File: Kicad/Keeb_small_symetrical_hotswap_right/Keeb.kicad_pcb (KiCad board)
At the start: 2 copper layers, 96.3 x 99.3 mm, 20 parts, among them J1 TYPE-C-31-M-12, SW1 CherryMX, SW10 CherryMX, SW11 CherryMX, SW13 CherryMX, SW14 CherryMX, SW15 CherryMX, SW16 CherryMX, SW17 CherryMX, SW18 CherryMX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

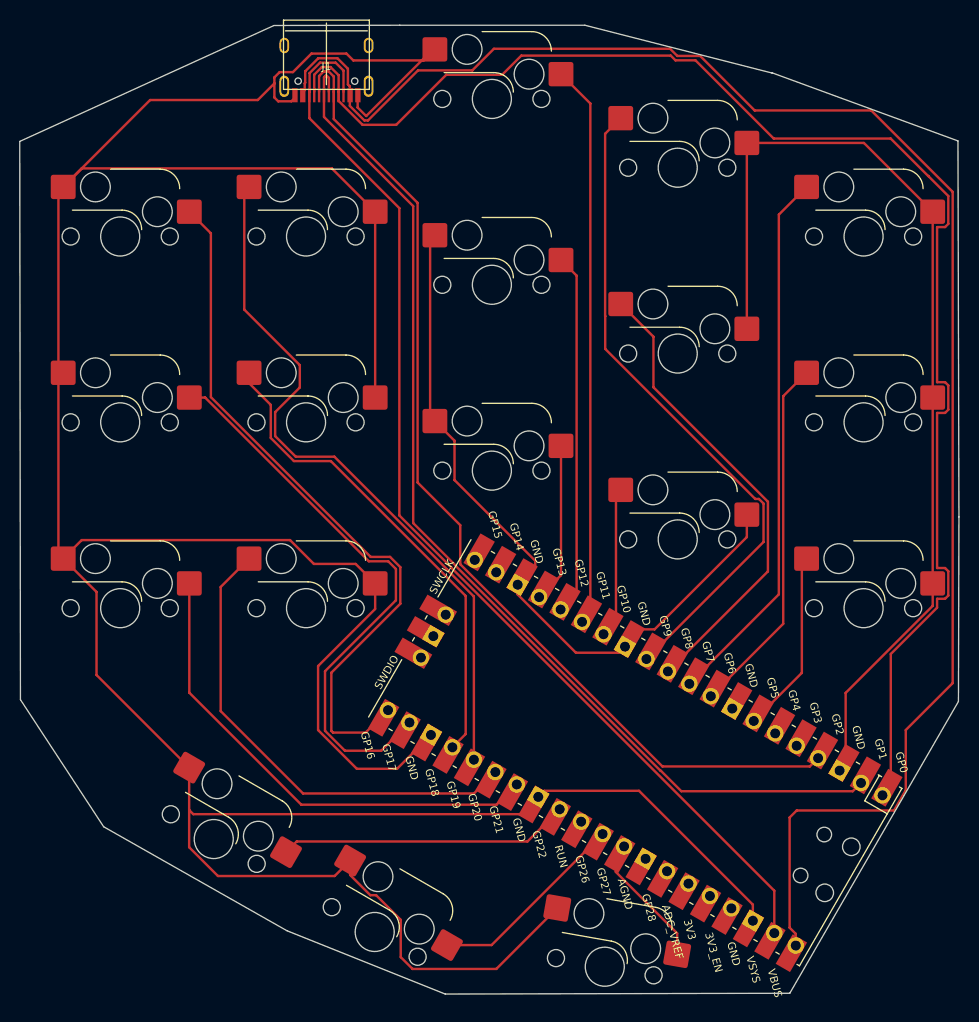
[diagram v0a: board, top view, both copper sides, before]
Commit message: Started work on the right half, fixed routing in the left half
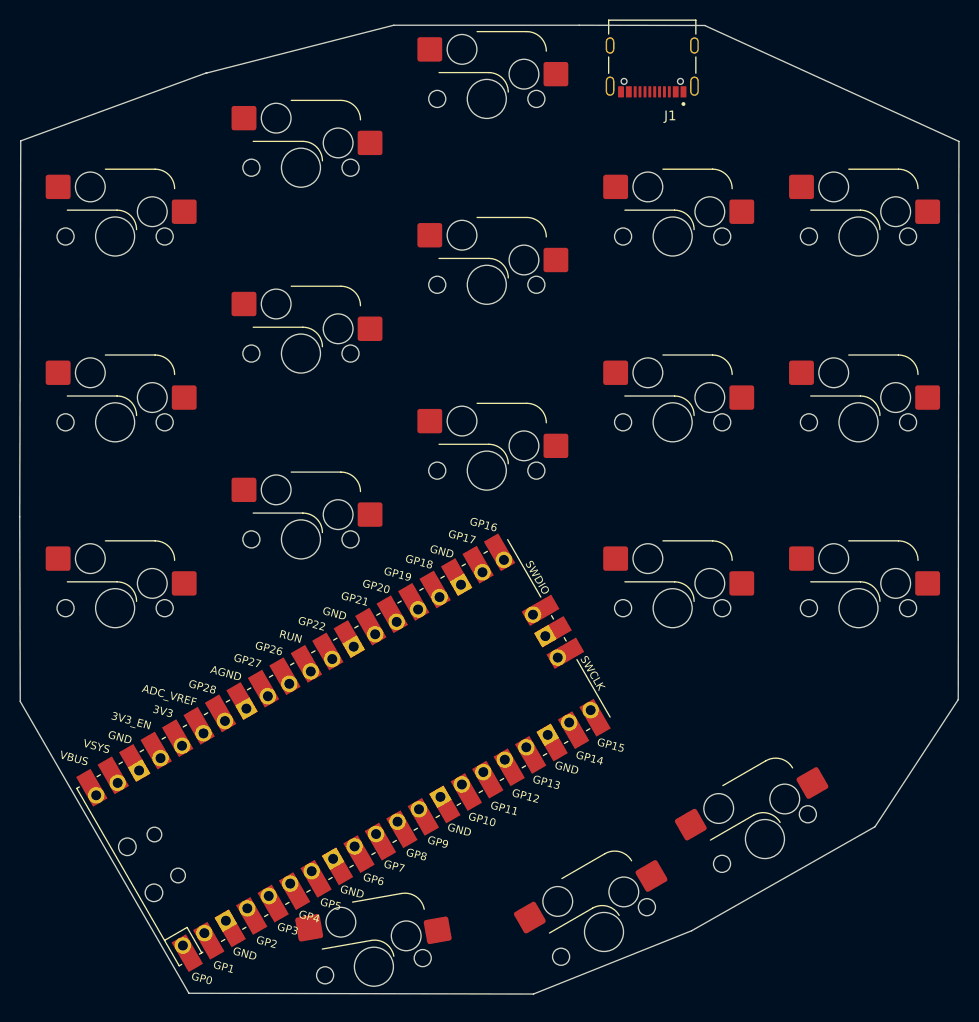
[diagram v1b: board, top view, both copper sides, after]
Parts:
- J1: footprint USB-C-Power-tester:TYPE-C-31-M-12 -> TypeC:HRO_TYPE-C-31-M-12
- moved SW3 76.7 mm to (111.6, 55.6)
- moved SW4 76.7 mm to (111.6, 74.7)
- moved SW5 76.7 mm to (111.6, 93.7)
- moved SW17 75.7 mm to (187.8, 55.6)
- moved SW18 75.7 mm to (187.8, 74.7)
- moved SW19 75.7 mm to (187.8, 93.7)
- moved SW20 56.5 mm to (178.2, 117.4), turned to -150 degrees
- moved SW6 38.6 mm to (130.7, 48.6)
- moved SW7 38.6 mm to (130.7, 67.6)
- moved SW8 38.6 mm to (130.7, 86.7)
- moved SW13 37.6 mm to (168.8, 55.6)
- moved SW14 37.6 mm to (168.8, 74.7)
- moved SW15 37.6 mm to (168.8, 93.7)
- moved J1 33.4 mm to (166.7, 36.0)
- moved U1 29.9 mm to (135.0, 108.5), turned to 120 degrees
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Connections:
- SW10 pad 1: 12 -> 11
- SW11 pad 1: 13 -> 12
- SW8 pad 2: 10 -> unconnected-(SW8-Pad2)
- SW9 pad 1: 11 -> 10
- U1 pad 41: (no net) -> unconnected-(U1-SWCLK-Pad41)
- U1 pad 42: (no net) -> unconnected-(U1-GND-Pad42)
- U1 pad 43: (no net) -> unconnected-(U1-SWDIO-Pad43)
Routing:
- net GND: track 549.3 -> 0.00 mm
- net 3v3: track 173.1 -> 0.00 mm
- net 0: track 148.5 -> 0.00 mm
- net VSYS: track 114.3 -> 0.00 mm
- net 1: track 109.2 -> 0.00 mm
- net 2: track 104.5 -> 0.00 mm
- net 16: track 73.1 -> 0.00 mm
- net 19: track 73.1 -> 0.00 mm
- net 9: track 68.0 -> 0.00 mm
- net 17: track 58.8 -> 0.00 mm
- net 11: track 57.7 -> 0.00 mm
- net 7: track 55.9 -> 0.00 mm
- net 21: track 50.4 -> 0.00 mm
- net 18: track 50.4 -> 0.00 mm
- net 20: track 49.4 -> 0.00 mm
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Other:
- outline, holes or cut-outs redrawn

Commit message: MVP of the right half
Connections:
- J1 pad A4_B9: 3v3 -> VSYS
- J1 pad B4_A9: 3v3 -> VSYS
- J1 pad B5: VSYS -> 3v3
- J1 pad B8: VSYS -> 3v3
- SW1 pad 1: 27 -> 4
- SW10 pad 1: 11 -> 17
- SW11 pad 1: 12 -> 16
- SW13 pad 2: 19 -> 13
- SW14 pad 2: 18 -> 12
- SW15 pad 2: 20 -> 11
- SW16 pad 1: 26 -> 5
- SW17 pad 1: 16 -> 9
- SW18 pad 1: 17 -> 8
- SW19 pad 1: 21 -> 7
- SW20 pad 1: 22 -> 6
- SW3 pad 2: 7 -> 26
- SW4 pad 2: 6 -> 27
- SW5 pad 2: 5 -> 28
- SW6 pad 2: 9 -> 21
- SW7 pad 2: 8 -> 20
- SW8 pad 2: unconnected-(SW8-Pad2) -> 19
- SW9 pad 1: 10 -> 18
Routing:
- net GND: track 0.00 -> 643.8 mm
- net 3v3: track 0.00 -> 117.2 mm
- net VSYS: track 0.00 -> 116.2 mm
- net 0: track 0.00 -> 114.3 mm
- net 1: track 0.00 -> 109.4 mm
- net 2: track 0.00 -> 107.0 mm
- net 9: track 0.00 -> 100.8 mm
- net 8: track 0.00 -> 86.1 mm
- net 13: track 0.00 -> 77.1 mm
- net 7: track 0.00 -> 70.0 mm
- net 26: track 0.00 -> 65.4 mm
- net 21: track 0.00 -> 63.7 mm
- net 12: track 0.00 -> 62.8 mm
- net 18: track 0.00 -> 61.9 mm
- net 6: track 0.00 -> 52.0 mm
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
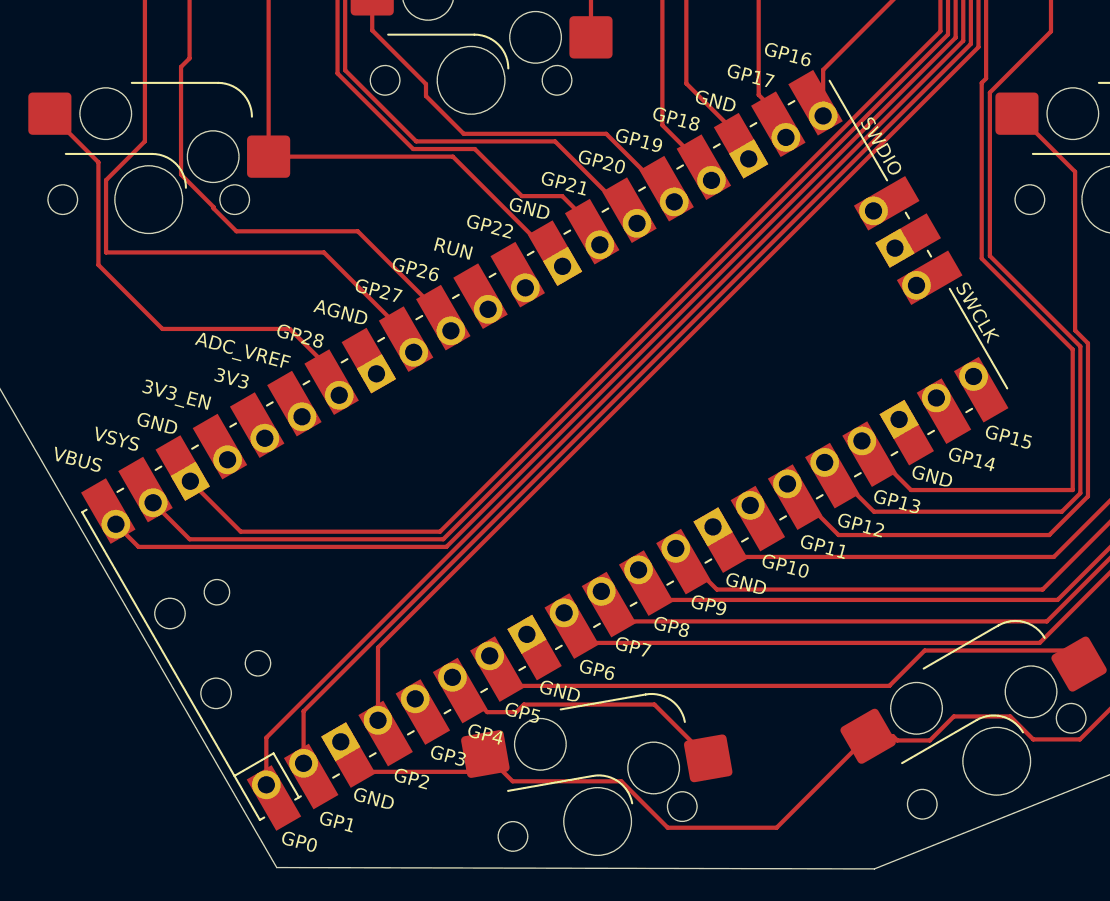
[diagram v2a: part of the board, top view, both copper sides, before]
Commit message: rm holes for controller
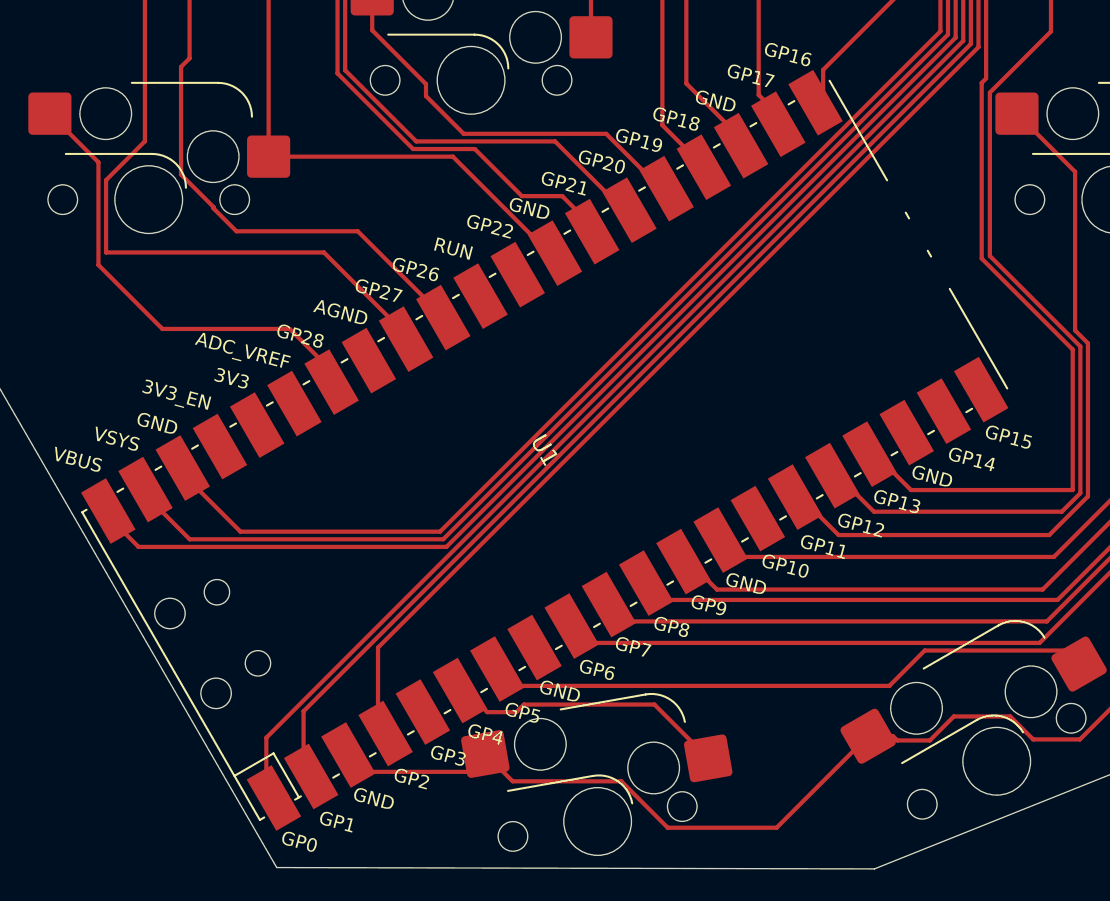
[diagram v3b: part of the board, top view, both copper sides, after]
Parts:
- U1: footprint MCU_RaspberryPi_and_Boards:RPi_Pico_SMD_TH -> MCU_RaspberryPi_and_Boards:RPi_Pico_SMD_TH_NO_HOLES

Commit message: Added mounting holes to the PCB
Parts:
- added H1: MountingHole, MountingHole:MountingHole_3.2mm_M3, B.Cu at (178.3, 46.1)
- added H2: MountingHole, MountingHole:MountingHole_3.2mm_M3, B.Cu at (140.2, 70.1)
- added H3: MountingHole, MountingHole:MountingHole_3.2mm_M3, B.Cu at (140.2, 51.0)
- added H4: MountingHole, MountingHole:MountingHole_3.2mm_M3, B.Cu at (121.1, 58.1)
- added H5: MountingHole, MountingHole:MountingHole_3.2mm_M3, B.Cu at (181.7, 104.4)
- added H7: MountingHole, MountingHole:MountingHole_3.2mm_M3, B.Cu at (178.3, 84.2)
- added H8: MountingHole, MountingHole:MountingHole_3.2mm_M3, B.Cu at (121.1, 96.2)
- added H9: MountingHole, MountingHole:MountingHole_3.2mm_M3, B.Cu at (148.7, 123.4)
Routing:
- net GND: track 643.8 -> 650.7 mm
- net 26: track 65.4 -> 68.8 mm
- net 27: track 51.9 -> 53.8 mm
- net 28: track 28.1 -> 29.7 mm
- net 9: track 100.8 -> 99.8 mm
- net 5: track 36.8 -> 37.3 mm
